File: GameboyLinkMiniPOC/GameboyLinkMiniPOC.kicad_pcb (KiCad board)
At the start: 2 copper layers, 39 x 34.5 mm, 6 parts, among them J2 AVR-ISP-6, SW1 SW_Reset, U1 ATtiny2313-20S

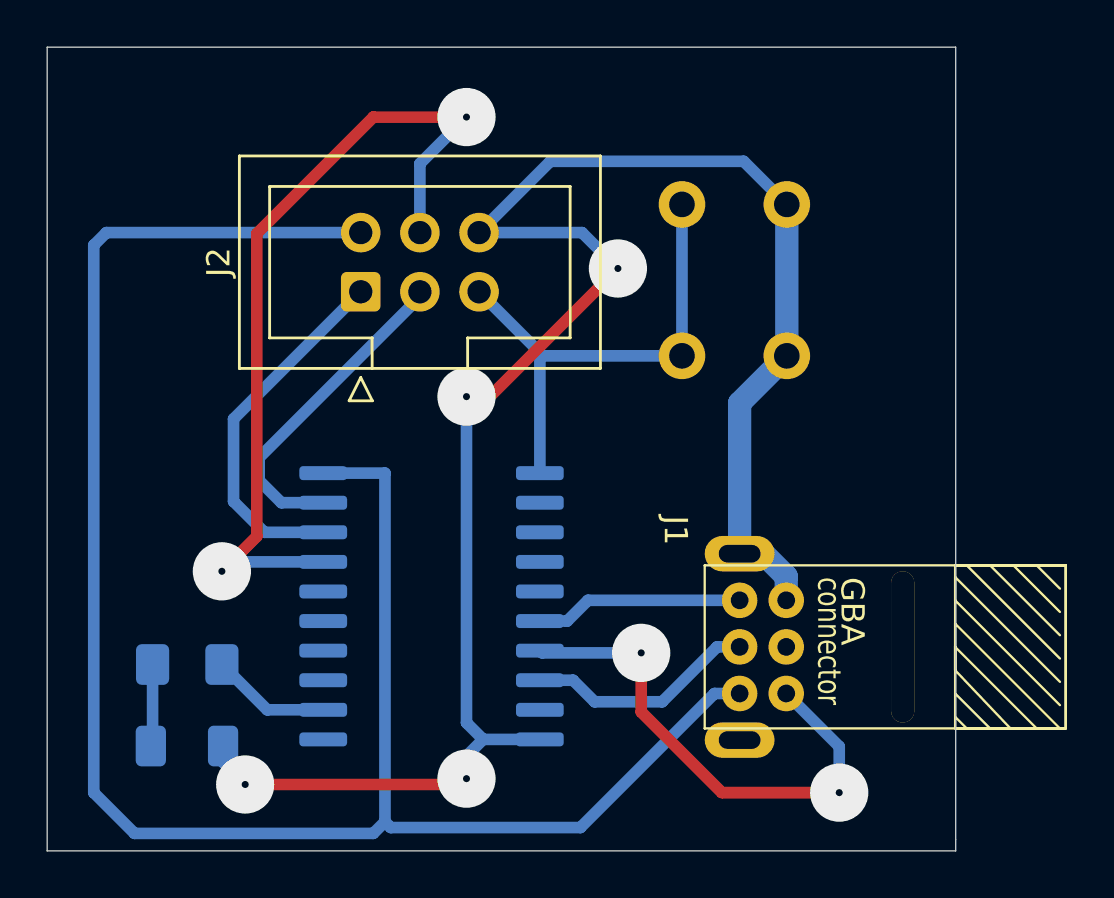
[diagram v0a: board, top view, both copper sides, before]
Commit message: Fixed passing (trench) of the GBA/Color Link connector, fixed the GB link mini PoC, resumed on the Link Mini.
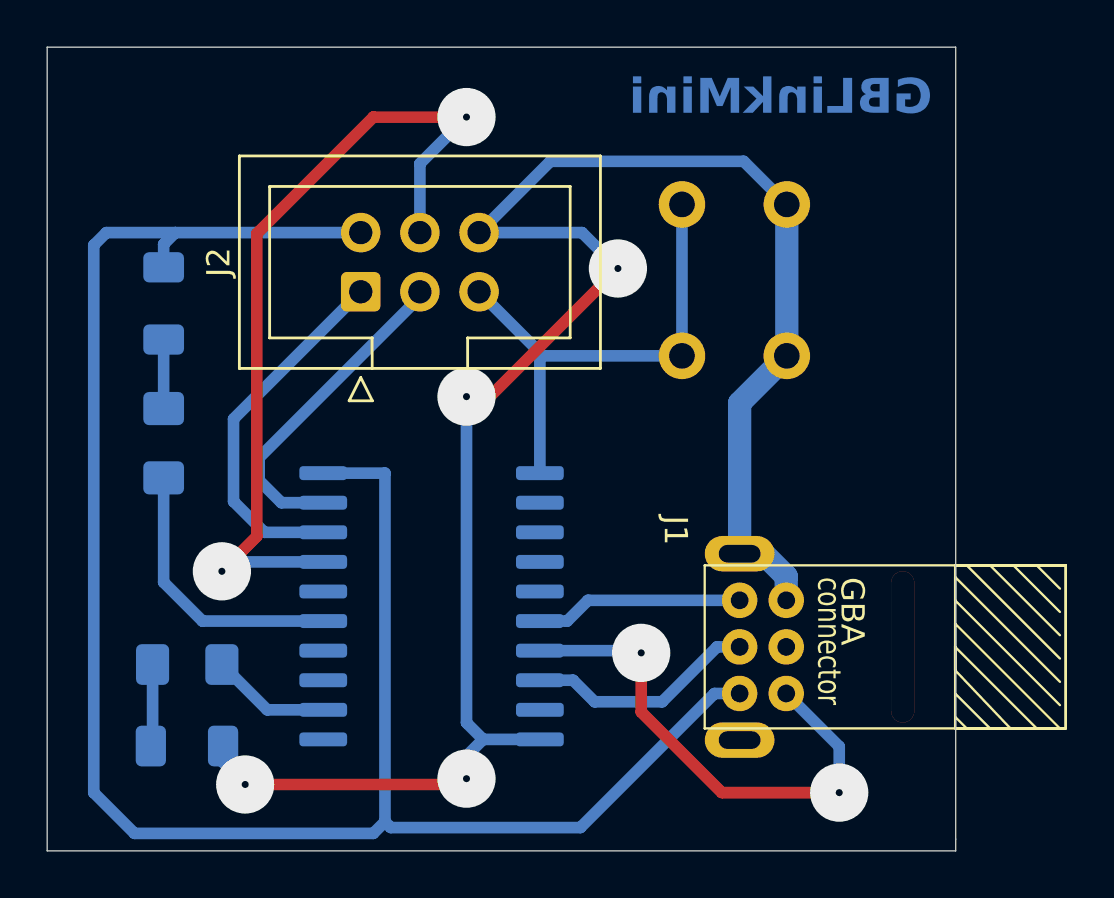
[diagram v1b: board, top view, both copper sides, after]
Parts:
- added D1: LED, LED_SMD:LED_1206_3216Metric_Pad1.42x1.75mm_HandSolder, B.Cu at (135.0, 79.5)
- added R2: R, Resistor_SMD:R_1206_3216Metric_Pad1.30x1.75mm_HandSolder, B.Cu at (135.0, 73.5)
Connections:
- U1 pad 15: (no net) -> unconnected-(D1-K-Pad1)
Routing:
- net unconnected-(D1-K-Pad1): track 0.00 -> 12.0 mm
- net Net-(D1-A): track 0.00 -> 2.96 mm
- net /VCC: track 83.9 -> 85.6 mm
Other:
- board text added: "GBLinkMini"
